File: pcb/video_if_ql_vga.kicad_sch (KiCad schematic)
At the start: 16 parts, among them J1 Conn_01x05, J2 DB15_Female_HighDensity, U1 SC0915

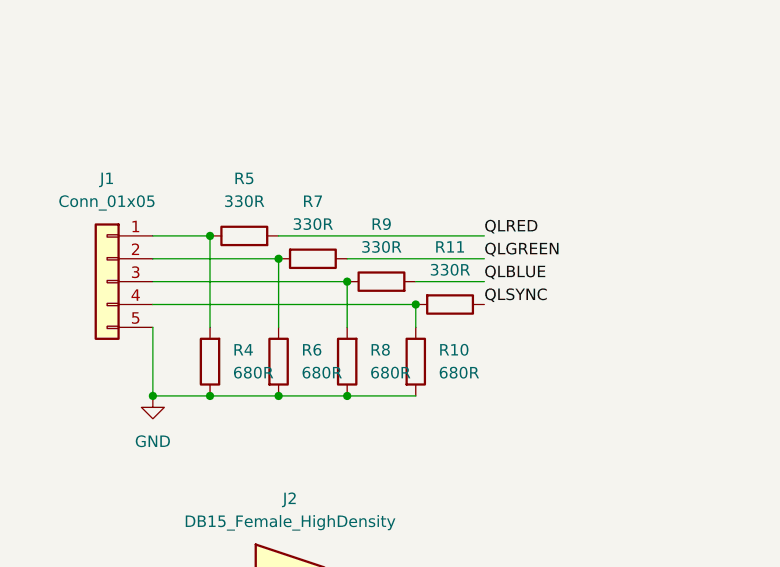
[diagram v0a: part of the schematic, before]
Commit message: Fix mistake in voltage divider
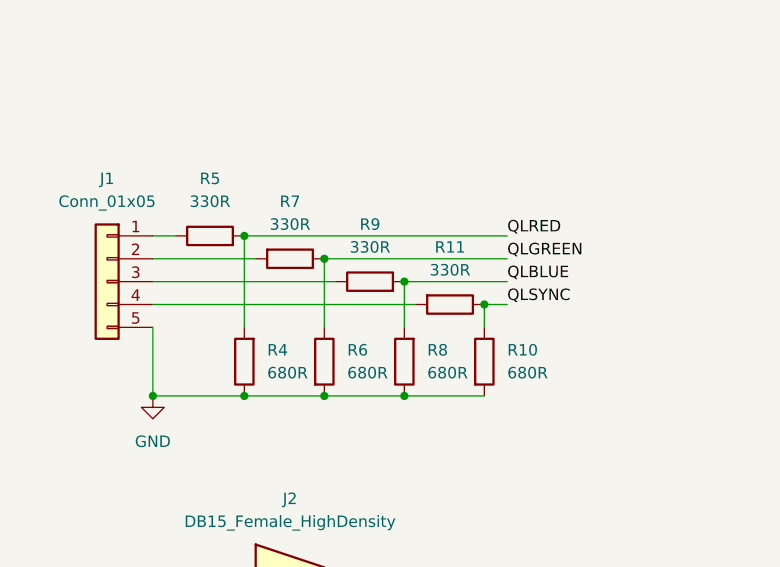
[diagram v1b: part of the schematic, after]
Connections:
- net QLBLUE: now also R8.2
- net QLGREEN: now also R6.1
- net QLRED: now also R4.2
- net QLSYNC: now also R10.1
- net at J1.1 (Pin_1), R5.1: no longer R4.2
- net at J1.2 (Pin_2), R7.2: no longer R6.1
- net at J1.4 (Pin_4), R11.2: no longer R10.1
- net at J1.3 (Pin_3), R9.1: no longer R8.2
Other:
- moved on the sheet: R10, R4, R5, R6, R7, R8, R9

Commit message: Add smd footprints for resistors
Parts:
- R1, R10, R11, R12, R13, R2, R3, R4, R5, R6, R7, R8, R9: footprint Resistor_THT:R_Axial_DIN0207_L6.3mm_D2.5mm_P7.62mm_Horizontal -> THT_SMD:R_Axial_DIN0207_L6.3mm_D2.5mm_P7.62_Horizontal
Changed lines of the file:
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@@
       (effects (font (size 1.27 1.27)) (justify right))
     )
-    (property "Footprint" "Resistor_THT:R_Axial_DIN0207_L6.3mm_D2.5mm_P7.62mm_Horizontal" (id 2) (at 110.998 74.93 90)
+    (property "Footprint" "THT_SMD:R_Axial_DIN0207_L6.3mm_D2.5mm_P7.62_Horizontal" (id 2) (at 110.998 74.93 90)
       (effects (font (size 1.27 1.27)) hide)
     )
@@
     (property "Reference" "R7" (id 0) (at 114.3 57.15 90))
     (property "Value" "330R" (id 1) (at 114.3 59.69 90))
-    (property "Footprint" "Resistor_THT:R_Axial_DIN0207_L6.3mm_D2.5mm_P7.62mm_Horizontal" (id 2) (at 114.3 61.722 90)
+    (property "Footprint" "THT_SMD:R_Axial_DIN0207_L6.3mm_D2.5mm_P7.62_Horizontal" (id 2) (at 114.3 61.722 90)
       (effects (font (size 1.27 1.27)) hide)
     )
@@
     (property "Reference" "R11" (id 0) (at 132.08 62.23 90))
     (property "Value" "330R" (id 1) (at 132.08 64.77 90))
-    (property "Footprint" "Resistor_THT:R_Axial_DIN0207_L6.3mm_D2.5mm_P7.62mm_Horizontal" (id 2) (at 132.08 66.802 90)
+    (property "Footprint" "THT_SMD:R_Axial_DIN0207_L6.3mm_D2.5mm_P7.62_Horizontal" (id 2) (at 132.08 66.802 90)
       (effects (font (size 1.27 1.27)) hide)
     )
@@
     (property "Reference" "R3" (id 0) (at 101.6 111.76 90))
     (property "Value" "330R" (id 1) (at 100.33 114.3 90))
-    (property "Footprint" "Resistor_THT:R_Axial_DIN0207_L6.3mm_D2.5mm_P7.62mm_Horizontal" (id 2) (at 95.25 114.808 90)
+    (property "Footprint" "THT_SMD:R_Axial_DIN0207_L6.3mm_D2.5mm_P7.62_Horizontal" (id 2) (at 95.25 114.808 90)
       (effects (font (size 1.27 1.27)) hide)
     )
@@
       (effects (font (size 1.27 1.27)) (justify right))
     )
-    (property "Footprint" "Resistor_THT:R_Axial_DIN0207_L6.3mm_D2.5mm_P7.62mm_Horizontal" (id 2) (at 128.778 74.93 90)
+    (property "Footprint" "THT_SMD:R_Axial_DIN0207_L6.3mm_D2.5mm_P7.62_Horizontal" (id 2) (at 128.778 74.93 90)
       (effects (font (size 1.27 1.27)) hide)
     )
@@
     (property "Reference" "R9" (id 0) (at 123.19 59.69 90))
     (property "Value" "330R" (id 1) (at 123.19 62.23 90))
-    (property "Footprint" "Resistor_THT:R_Axial_DIN0207_L6.3mm_D2.5mm_P7.62mm_Horizontal" (id 2) (at 123.19 67.818 90)
+    (property "Footprint" "THT_SMD:R_Axial_DIN0207_L6.3mm_D2.5mm_P7.62_Horizontal" (id 2) (at 123.19 67.818 90)
       (effects (font (size 1.27 1.27)) hide)
     )
@@
     (property "Reference" "R5" (id 0) (at 105.41 54.61 90))
     (property "Value" "330R" (id 1) (at 105.41 57.15 90))
-    (property "Footprint" "Resistor_THT:R_Axial_DIN0207_L6.3mm_D2.5mm_P7.62mm_Horizontal" (id 2) (at 105.41 62.738 90)
+    (property "Footprint" "THT_SMD:R_Axial_DIN0207_L6.3mm_D2.5mm_P7.62_Horizontal" (id 2) (at 105.41 62.738 90)
       (effects (font (size 1.27 1.27)) hide)
     )
@@
     (property "Reference" "R2" (id 0) (at 101.6 106.68 90))
     (property "Value" "330R" (id 1) (at 100.33 109.22 90))
-    (property "Footprint" "Resistor_THT:R_Axial_DIN0207_L6.3mm_D2.5mm_P7.62mm_Horizontal" (id 2) (at 95.25 109.728 90)
+    (property "Footprint" "THT_SMD:R_Axial_DIN0207_L6.3mm_D2.5mm_P7.62_Horizontal" (id 2) (at 95.25 109.728 90)
       (effects (font (size 1.27 1.27)) hide)
     )
@@
       (effects (font (size 1.27 1.27)) (justify left))
     )
-    (property "Footprint" "Resistor_THT:R_Axial_DIN0207_L6.3mm_D2.5mm_P7.62mm_Horizontal" (id 2) (at 116.332 74.93 90)
+    (property "Footprint" "THT_SMD:R_Axial_DIN0207_L6.3mm_D2.5mm_P7.62_Horizontal" (id 2) (at 116.332 74.93 90)
       (effects (font (size 1.27 1.27)) hide)
     )
@@
     (property "Reference" "R12" (id 0) (at 127 111.76 90))
     (property "Value" "100R" (id 1) (at 125.73 114.3 90))
-    (property "Footprint" "Resistor_THT:R_Axial_DIN0207_L6.3mm_D2.5mm_P7.62mm_Horizontal" (id 2) (at 133.35 114.808 90)
+    (property "Footprint" "THT_SMD:R_Axial_DIN0207_L6.3mm_D2.5mm_P7.62_Horizontal" (id 2) (at 133.35 114.808 90)
       (effects (font (size 1.27 1.27)) hide)
     )
@@
     (property "Reference" "R13" (id 0) (at 127 116.84 90))
     (property "Value" "100R" (id 1) (at 125.73 119.38 90))
-    (property "Footprint" "Resistor_THT:R_Axial_DIN0207_L6.3mm_D2.5mm_P7.62mm_Horizontal" (id 2) (at 133.35 119.888 90)
+    (property "Footprint" "THT_SMD:R_Axial_DIN0207_L6.3mm_D2.5mm_P7.62_Horizontal" (id 2) (at 133.35 119.888 90)
       (effects (font (size 1.27 1.27)) hide)
     )
@@
     (property "Reference" "R1" (id 0) (at 101.6 101.6 90))
     (property "Value" "330R" (id 1) (at 100.33 104.14 90))
-    (property "Footprint" "Resistor_THT:R_Axial_DIN0207_L6.3mm_D2.5mm_P7.62mm_Horizontal" (id 2) (at 95.25 104.648 90)
+    (property "Footprint" "THT_SMD:R_Axial_DIN0207_L6.3mm_D2.5mm_P7.62_Horizontal" (id 2) (at 95.25 104.648 90)
       (effects (font (size 1.27 1.27)) hide)
     )
@@
       (effects (font (size 1.27 1.27)) (justify left))
     )
-    (property "Footprint" "Resistor_THT:R_Axial_DIN0207_L6.3mm_D2.5mm_P7.62mm_Horizontal" (id 2) (at 134.112 74.93 90)
+    (property "Footprint" "THT_SMD:R_Axial_DIN0207_L6.3mm_D2.5mm_P7.62_Horizontal" (id 2) (at 134.112 74.93 90)
       (effects (font (size 1.27 1.27)) hide)
     )
@@
     )
     (path "/d6c5748c-4745-4d80-a9b6-2ee84d01cbab"
-      (reference "R1") (unit 1) (value "330R") (footprint "Resistor_THT:R_Axial_DIN0207_L6.3mm_D2.5mm_P7.62mm_Horizontal")
+      (reference "R1") (unit 1) (value "330R") (footprint "THT_SMD:R_Axial_DIN0207_L6.3mm_D2.5mm_P7.62_Horizontal")
     )
     (path "/7380ae29-9f8b-4e41-bbcb-d1fafe936a05"
-      (reference "R2") (unit 1) (value "330R") (footprint "Resistor_THT:R_Axial_DIN0207_L6.3mm_D2.5mm_P7.62mm_Horizontal")
+      (reference "R2") (unit 1) (value "330R") (footprint "THT_SMD:R_Axial_DIN0207_L6.3mm_D2.5mm_P7.62_Horizontal")
     )
     (path "/3461f2da-9e2a-422d-9290-0b1570f34fce"
-      (reference "R3") (unit 1) (value "330R") (footprint "Resistor_THT:R_Axial_DIN0207_L6.3mm_D2.5mm_P7.62mm_Horizontal")
+      (reference "R3") (unit 1) (value "330R") (footprint "THT_SMD:R_Axial_DIN0207_L6.3mm_D2.5mm_P7.62_Horizontal")
     )
     (path "/09fd8705-9a88-44e8-819a-62b26c78a4b6"
-      (reference "R4") (unit 1) (value "680R") (footprint "Resistor_THT:R_Axial_DIN0207_L6.3mm_D2.5mm_P7.62mm_Horizontal")
+      (reference "R4") (unit 1) (value "680R") (footprint "THT_SMD:R_Axial_DIN0207_L6.3mm_D2.5mm_P7.62_Horizontal")
     )
     (path "/62f233a1-c1d7-4ed8-8a2f-4b67ed8f2aef"
-      (reference "R5") (unit 1) (value "330R") (footprint "Resistor_THT:R_Axial_DIN0207_L6.3mm_D2.5mm_P7.62mm_Horizontal")
+      (reference "R5") (unit 1) (value "330R") (footprint "THT_SMD:R_Axial_DIN0207_L6.3mm_D2.5mm_P7.62_Horizontal")
     )
     (path "/9a162d62-582b-4c45-a88d-59b485be820a"
-      (reference "R6") (unit 1) (value "680R") (footprint "Resistor_THT:R_Axial_DIN0207_L6.3mm_D2.5mm_P7.62mm_Horizontal")
+      (reference "R6") (unit 1) (value "680R") (footprint "THT_SMD:R_Axial_DIN0207_L6.3mm_D2.5mm_P7.62_Horizontal")
     )
     (path "/0cde47c1-b37e-4555-87c1-ff53acb95fe8"
-      (reference "R7") (unit 1) (value "330R") (footprint "Resistor_THT:R_Axial_DIN0207_L6.3mm_D2.5mm_P7.62mm_Horizontal")
+      (reference "R7") (unit 1) (value "330R") (footprint "THT_SMD:R_Axial_DIN0207_L6.3mm_D2.5mm_P7.62_Horizontal")
     )
     (path "/4298e4ef-9eea-45a8-adbc-b088b698be7c"
-      (reference "R8") (unit 1) (value "680R") (footprint "Resistor_THT:R_Axial_DIN0207_L6.3mm_D2.5mm_P7.62mm_Horizontal")
+      (reference "R8") (unit 1) (value "680R") (footprint "THT_SMD:R_Axial_DIN0207_L6.3mm_D2.5mm_P7.62_Horizontal")
     )
     (path "/4a4a614f-1d7e-4e88-b815-ba2c20ac5b5b"
-      (reference "R9") (unit 1) (value "330R") (footprint "Resistor_THT:R_Axial_DIN0207_L6.3mm_D2.5mm_P7.62mm_Horizontal")
+      (reference "R9") (unit 1) (value "330R") (footprint "THT_SMD:R_Axial_DIN0207_L6.3mm_D2.5mm_P7.62_Horizontal")
     )
     (path "/db41563a-815f-4ebc-9635-2889ff312352"
-      (reference "R10") (unit 1) (value "680R") (footprint "Resistor_THT:R_Axial_DIN0207_L6.3mm_D2.5mm_P7.62mm_Horizontal")
+      (reference "R10") (unit 1) (value "680R") (footprint "THT_SMD:R_Axial_DIN0207_L6.3mm_D2.5mm_P7.62_Horizontal")
     )
     (path "/1476d52d-3844-463c-85fb-a6a7866f8dbf"
-      (reference "R11") (unit 1) (value "330R") (footprint "Resistor_THT:R_Axial_DIN0207_L6.3mm_D2.5mm_P7.62mm_Horizontal")
+      (reference "R11") (unit 1) (value "330R") (footprint "THT_SMD:R_Axial_DIN0207_L6.3mm_D2.5mm_P7.62_Horizontal")
     )
     (path "/ca48dd38-2f75-4057-9e30-d6c203acc6d4"
-      (reference "R12") (unit 1) (value "100R") (footprint "Resistor_THT:R_Axial_DIN0207_L6.3mm_D2.5mm_P7.62mm_Horizontal")
+      (reference "R12") (unit 1) (value "100R") (footprint "THT_SMD:R_Axial_DIN0207_L6.3mm_D2.5mm_P7.62_Horizontal")
     )
     (path "/cd0102a1-4ba3-47f2-a595-52a36cad0c3f"
-      (reference "R13") (unit 1) (value "100R") (footprint "Resistor_THT:R_Axial_DIN0207_L6.3mm_D2.5mm_P7.62mm_Horizontal")
+      (reference "R13") (unit 1) (value "100R") (footprint "THT_SMD:R_Axial_DIN0207_L6.3mm_D2.5mm_P7.62_Horizontal")
     )
     (path "/9feac91f-fab8-4de5-bcbb-ba5e1feb9d90"
